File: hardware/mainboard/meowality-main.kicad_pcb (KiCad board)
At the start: 6 copper layers, 175 x 85 mm, 249 parts, among them J1 Micro_SD_Card_Det, J2 MINI_DP_SINK, J3 DEBUG, J4 USB_C_Receptacle, P1 M2_SOCKET_E, Q1 BSS138, Q10 BSS138, Q2 BSS138, Q3 BSS138, Q4 BSS138, Q5 BSS138, Q6 FDN340P, Q7 BSS138, SW1 SW_DIP_x04, SW2 SW_Push, SW3 SW_Push, SW4 SW_Push, SW5 SW_Push, SW6 SW_Push, U1 CP3225-100.000-3.3-25-X-T-TR, U10 MMC5983MA, U11 Si52112-B, U12 TPD4E02B04DQA, U13 TPD4E02B04DQA, U14 CBTL02043A, U15 FUSB302B11MPX, U16 USB3318, U19 ADP5070ACPZ, U2 AX3HAF1-135.0000T, U20 CAT4106HV4, U21 74LVC2T45DC, U3 AP6230xWU, U4 AP6230xWU, U5 SiC438, U6 AP6230xWU, U7 AP6230xWU, U8 TXS02612, U9 ICM-20789, X1 831056169, Y1 25MHz

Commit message: Initial 'floorplan' outline
Signed-off-by: gatecat <gatecat@ds0.me>
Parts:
- added C65: 10µ, Capacitor_SMD:C_1206_3216Metric, F.Cu at (327.7, 106.7)
- added C66: 100n, Capacitor_SMD:C_0402_1005Metric, F.Cu at (331.9, 107.1)
- added C77: 22µ, Capacitor_SMD:C_1206_3216Metric, F.Cu at (320.5, 110.7)
- added C78: 22µ, Capacitor_SMD:C_1206_3216Metric, F.Cu at (327.7, 103.3)
- added H1: MountingHole_Pad, MountingHole:MountingHole_2.7mm_M2.5_Pad_Via, F.Cu at (33.0, 117.0)
- added H10: MountingHole_Pad, MountingHole:MountingHole_2.7mm_M2.5_Pad_Via, F.Cu at (53.0, 63.0)
- added H2: MountingHole_Pad, MountingHole:MountingHole_2.7mm_M2.5_Pad_Via, F.Cu at (74.0, 132.0)
- added H3: MountingHole_Pad, MountingHole:MountingHole_2.7mm_M2.5_Pad_Via, F.Cu at (227.0, 132.0)
- added H4: MountingHole_Pad, MountingHole:MountingHole_2.7mm_M2.5_Pad_Via, F.Cu at (227.0, 63.0)
- added H5: MountingHole_Pad, MountingHole:MountingHole_2.7mm_M2.5_Pad_Via, F.Cu at (227.0, 97.5)
- added H6: MountingHole_Pad, MountingHole:MountingHole_2.7mm_M2.5_Pad_Via, F.Cu at (118.1, 132.1)
- added H7: MountingHole_Pad, MountingHole:MountingHole_2.7mm_M2.5_Pad_Via, F.Cu at (190.0, 63.0)
- added H8: MountingHole_Pad, MountingHole:MountingHole_2.7mm_M2.5_Pad_Via, F.Cu at (67.0, 105.5)
- added H9: MountingHole_Pad, MountingHole:MountingHole_2.7mm_M2.5_Pad_Via, F.Cu at (140.0, 63.0)
- added L9: 3.3µ, meowality:BWVS00606045, F.Cu at (321.3, 105.4)
- added R28: 31.6k, Resistor_SMD:R_0402_1005Metric, F.Cu at (327.7, 109.3)
- added R97: 10k, Resistor_SMD:R_0402_1005Metric, F.Cu at (324.8, 110.0)
- added U17: AP6230xWU, Package_TO_SOT_SMD:TSOT-23-6, F.Cu at (333.1, 103.9)
- LCD1, LCD2: moved to B.Cu
- moved SW6 354.4 mm to (56.0, 100.0)
- moved SW3 348.2 mm to (56.0, 76.0)
- moved SW4 342.2 mm to (56.0, 84.0)
- moved SW5 342.2 mm to (56.0, 92.0)
- moved LCD1 283.3 mm to (100.0, 87.0), turned to -90 degrees
- moved U14 276.8 mm to (55.0, 114.0)
- moved U9 275.3 mm to (121.0, 105.0)
- moved LCD2 240.1 mm to (160.0, 87.0), turned to -90 degrees
- moved C9 202.3 mm to (67.0, 96.0), turned to 90 degrees
- moved U4 125.7 mm to (166.0, 125.0)
- moved L2 114.8 mm to (159.0, 127.0)
- moved C21 114.2 mm to (166.0, 129.0)
- moved SOM1 66.0 mm to (221.3, 64.2), turned to 180 degrees
- moved SW1 48.5 mm to (216.0, 129.0)
- moved CAM2 29.5 mm to (110.0, 71.0)
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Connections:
- CAM1 pad 22: +3V3PS -> +3V3PL
- CAM2 pad 22: +3V3PS -> +3V3PL
- R63 pad 1: +3V3PS -> +3V3PL
- R64 pad 1: +3V3PS -> +3V3PL
- R65 pad 1: +3V3PS -> +3V3PL
- R66 pad 1: +3V3PS -> +3V3PL
- SOM1 pad 2D59: +3V3PS -> +3V3PL
- SOM1 pad 2D60: +3V3PS -> +3V3PL
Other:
- board size 175 x 85 mm -> 200 x 75 mm

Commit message: Placement snapshot
Signed-off-by: gatecat <gatecat@ds0.me>
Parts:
- moved U8 347.1 mm to (70.6, 78.5)
- moved U15 264.0 mm to (78.1, 122.6)
- moved U16 250.2 mm to (92.4, 122.0)
- moved C10 229.7 mm to (73.5, 89.2), turned to -90 degrees
- moved C13 221.0 mm to (71.0, 89.2), turned to -90 degrees
- moved C15 211.5 mm to (75.8, 89.3), turned to -90 degrees
- moved U5 197.1 mm to (78.1, 87.0)
- moved L3 191.9 mm to (79.2, 97.2)
- moved C18 150.9 mm to (152.0, 123.2), turned to 180 degrees
- moved C12 145.8 mm to (147.0, 124.8), turned to 180 degrees
- moved R9 143.7 mm to (155.8, 128.0), turned to 90 degrees
- moved U2 136.4 mm to (139.5, 95.5)
- moved R10 135.8 mm to (155.8, 125.8), turned to 90 degrees
- moved C17 132.7 mm to (167.0, 123.2), turned to 180 degrees
- moved C30 126.1 mm to (182.0, 123.2), turned to 180 degrees
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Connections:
- U5 pad 12: /Power/SiC_V_{DD} -> Net-(C16-Pad2)
- U5 pad 15: (no net) -> /Power/SiC_V_{DD}

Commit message: Placement snapshot 2
Signed-off-by: gatecat <gatecat@ds0.me>
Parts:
- moved R80 333.3 mm to (86.2, 72.2)
- moved R79 325.3 mm to (86.2, 75.8)
- moved R76 318.9 mm to (101.2, 81.5), turned to 90 degrees
- moved R77 317.3 mm to (100.0, 81.5), turned to 90 degrees
- moved R78 315.1 mm to (86.2, 73.5)
- moved R87 314.8 mm to (99.0, 81.5), turned to -90 degrees
- moved L6 313.8 mm to (97.2, 70.0), turned to 90 degrees
- moved R75 313.5 mm to (95.8, 88.8)
- moved R88 311.0 mm to (103.0, 77.5)
- moved C73 308.6 mm to (103.0, 76.0)
- moved C70 308.6 mm to (96.0, 84.8), turned to 90 degrees
- moved C75 308.2 mm to (109.0, 68.5), turned to 90 degrees
- moved R86 304.6 mm to (94.8, 82.2), turned to 90 degrees
- moved R82 304.1 mm to (103.5, 81.0), turned to 90 degrees
- moved C74 303.6 mm to (91.8, 82.2)
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
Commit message: Placement snapshot 3
Signed-off-by: gatecat <gatecat@ds0.me>
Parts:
- removed the C65 at (302.2, 142.7)
- removed the C66 at (290.2, 153.4)
- removed Q4: BSS138, Package_TO_SOT_SMD:SOT-23
- removed Q6: FDN340P, Package_TO_SOT_SMD:SOT-23
- removed the R28 at (289.4, 157.7)
- TP2, TP3: moved to B.Cu
- moved R32 359.0 mm to (79.5, 64.2), turned to -90 degrees
- moved D7 354.4 mm to (73.5, 61.0)
- moved C40 345.9 mm to (70.8, 73.5), turned to 180 degrees
- moved D10 343.1 mm to (64.5, 61.0)
- moved R33 331.1 mm to (78.0, 64.2), turned to -90 degrees
- moved D9 331.0 mm to (69.0, 61.0)
- moved R23 329.3 mm to (113.8, 95.5), turned to 90 degrees
- moved R36 328.5 mm to (101.0, 97.2), turned to 180 degrees
- moved C42 326.8 mm to (74.8, 78.2), turned to -90 degrees
- moved R25 325.1 mm to (110.5, 103.8), turned to 90 degrees
- moved D6 324.3 mm to (78.0, 61.0)
- moved R37 324.3 mm to (101.0, 95.8), turned to 180 degrees
- moved C37 323.2 mm to (118.0, 101.0)
- moved C44 317.0 mm to (104.3, 98.8)
- moved C36 315.4 mm to (118.5, 99.5)
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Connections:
- C46 pad 1: Net-(C46-Pad1) -> unconnected-(C46-Pad1)
- C46 pad 2: GND -> unconnected-(C46-Pad2)
- C47 pad 1: Net-(C46-Pad1) -> unconnected-(C47-Pad1)
- C47 pad 2: GND -> unconnected-(C47-Pad2)
- D10 pad 2: Net-(D10-Pad2) -> unconnected-(D10-Pad2)
- FB2 pad 2: Net-(C46-Pad1) -> Net-(FB2-Pad2)
- R70 pad 1: Net-(D10-Pad2) -> unconnected-(R70-Pad1)
- R70 pad 2: PL_LED3B -> unconnected-(R70-Pad2)
- U11 pad 1: Net-(C46-Pad1) -> Net-(FB2-Pad2)
- U11 pad 10: Net-(C46-Pad1) -> Net-(FB2-Pad2)

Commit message: All parts placed
Signed-off-by: gatecat <gatecat@ds0.me>
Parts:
- R52, R53: value 5.1k -> DNP
- TP1: moved to B.Cu
- moved R42 374.5 mm to (62.0, 73.2), turned to -90 degrees
- moved R39 373.3 mm to (65.8, 83.2)
- moved R96 373.2 mm to (58.5, 64.2), turned to -90 degrees
- moved R71 369.1 mm to (64.5, 64.2), turned to -90 degrees
- moved R70 363.9 mm to (65.8, 64.2), turned to -90 degrees
- moved C35 359.3 mm to (66.0, 77.2), turned to 90 degrees
- moved R41 357.9 mm to (84.2, 130.8)
- moved R95 355.5 mm to (59.8, 64.2), turned to -90 degrees
- moved R69 350.7 mm to (67.8, 64.2), turned to -90 degrees
- moved R40 348.8 mm to (74.5, 64.2), turned to -90 degrees
- moved R73 348.6 mm to (61.0, 64.2), turned to -90 degrees
- moved R49 346.5 mm to (72.0, 64.2), turned to -90 degrees
- moved R72 342.8 mm to (63.2, 64.2), turned to -90 degrees
- moved R67 342.3 mm to (70.2, 64.2), turned to -90 degrees
- moved R48 341.6 mm to (73.2, 64.2), turned to -90 degrees
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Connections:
- C46 pad 1: unconnected-(C46-Pad1) -> Net-(FB2-Pad2)
- C46 pad 2: unconnected-(C46-Pad2) -> GND
- C47 pad 1: unconnected-(C47-Pad1) -> Net-(FB2-Pad2)
- C47 pad 2: unconnected-(C47-Pad2) -> GND
- C54 pad 1: /IO/SSTXC1+ -> /IO/SSTX1+
- C55 pad 1: /IO/SSTXC1- -> /IO/SSTX1-
- C56 pad 1: /IO/SSTXC2+ -> /IO/SSTX2+
- C57 pad 1: /IO/SSTXC2- -> /IO/SSTX2-
- D10 pad 2: unconnected-(D10-Pad2) -> Net-(D10-Pad2)
- R70 pad 1: unconnected-(R70-Pad1) -> Net-(D10-Pad2)
- R70 pad 2: unconnected-(R70-Pad2) -> PL_LED3B
- U5 pad 12: Net-(C16-Pad2) -> /Power/SiC_V_{DD}
- U5 pad 15: /Power/SiC_V_{DD} -> (no net)

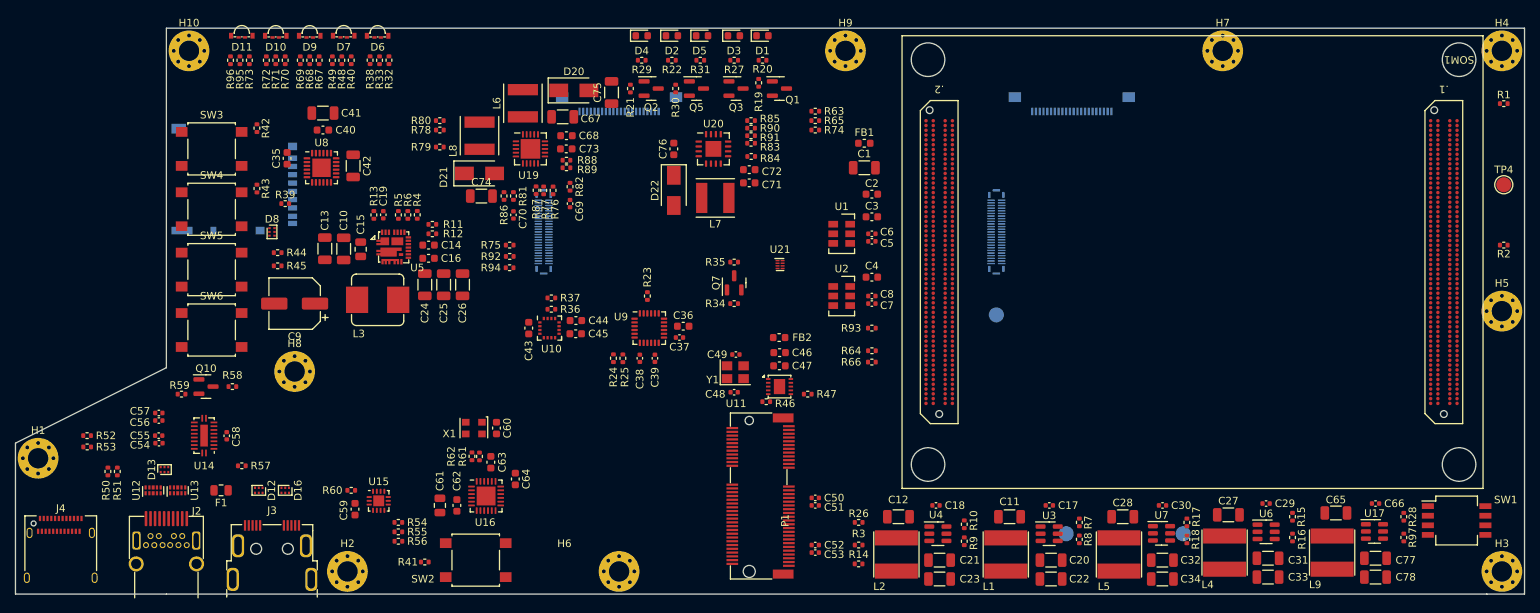
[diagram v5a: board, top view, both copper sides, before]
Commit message: Tidy up silk
Signed-off-by: gatecat <gatecat@ds0.me>
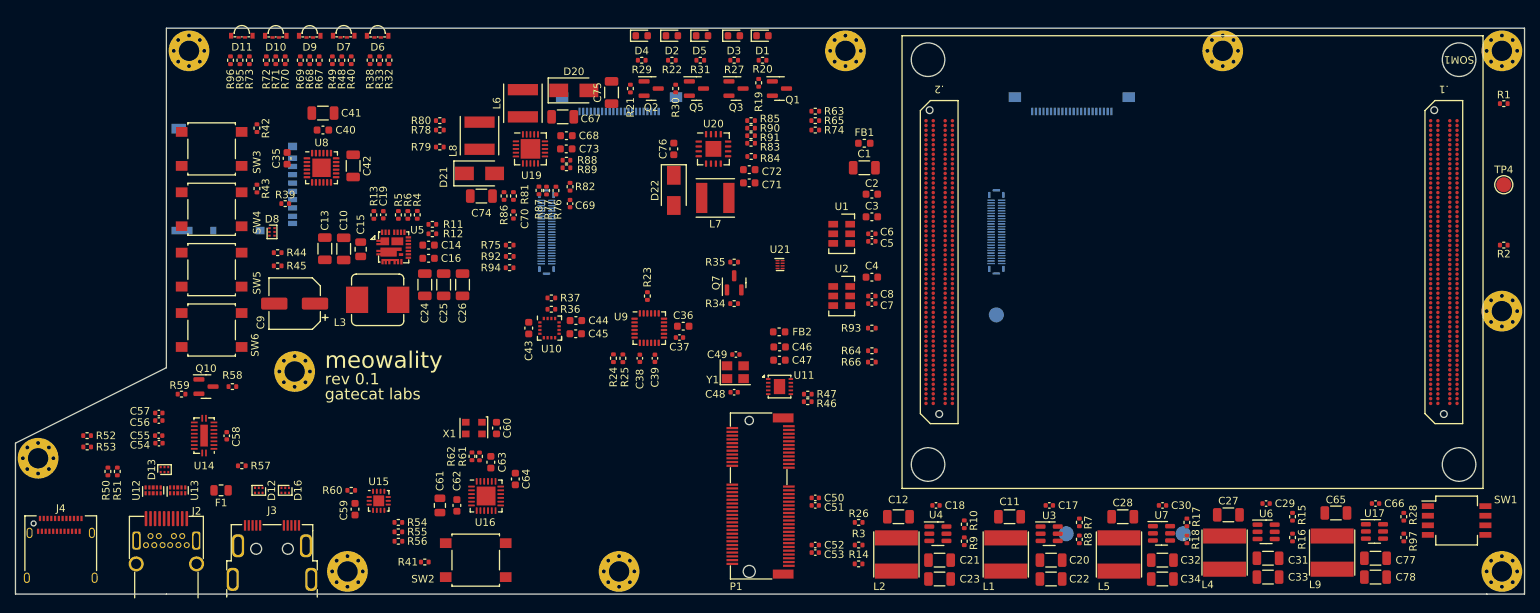
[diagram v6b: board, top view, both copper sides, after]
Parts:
- moved R46 5.50 mm to (135.0, 109.5)
- moved C46 0.75 mm to (131.3, 102.2)
- moved C47 0.75 mm to (131.2, 104.0)
- moved FB2 0.75 mm to (131.2, 100.2)
- moved LCD1 0.38 mm to (100.4, 87.0)
- moved R76 0.38 mm to (101.6, 81.5)
- moved R77 0.38 mm to (100.4, 81.5)
- moved R87 0.38 mm to (99.4, 81.5)
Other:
- board text added: "gatecat labs"
- board text added: "meowality"
- board text added: "rev 0.1"

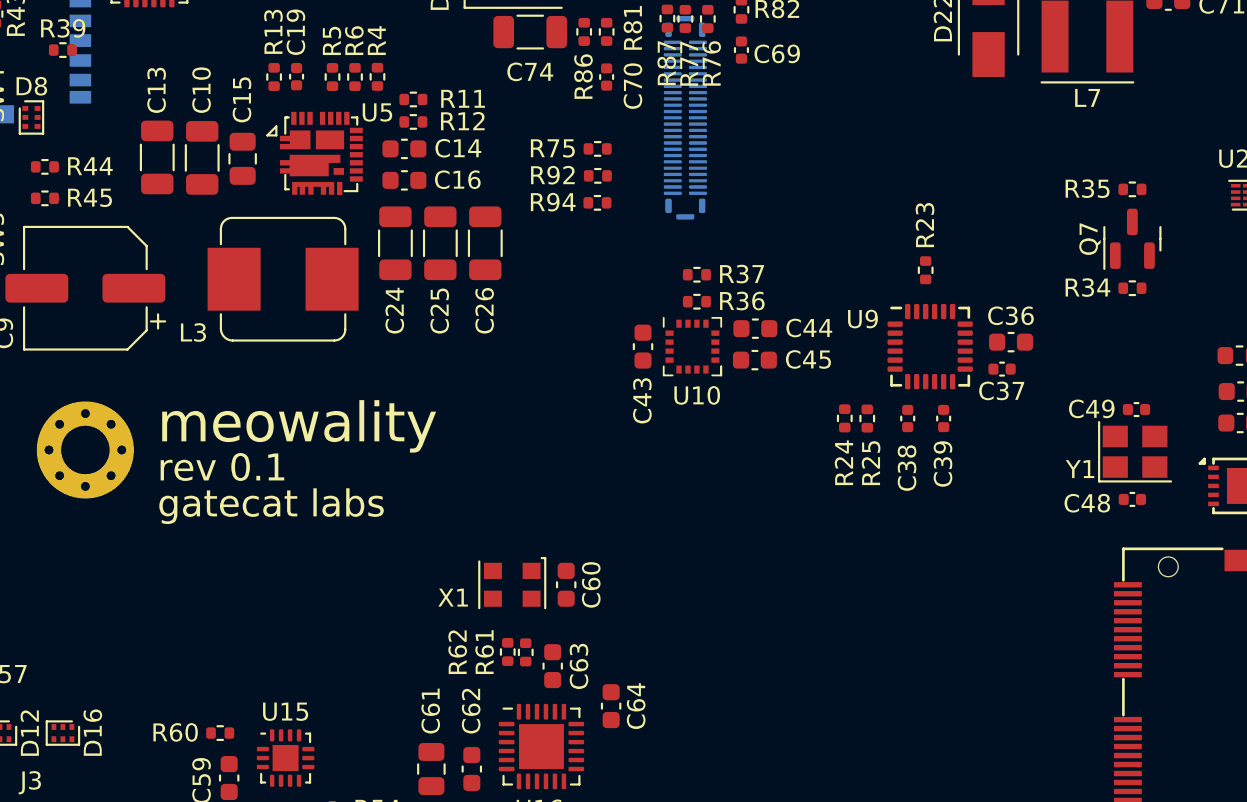
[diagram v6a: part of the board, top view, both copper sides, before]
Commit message: Add TVS on 5V and Vbus
Signed-off-by: gatecat <gatecat@ds0.me>
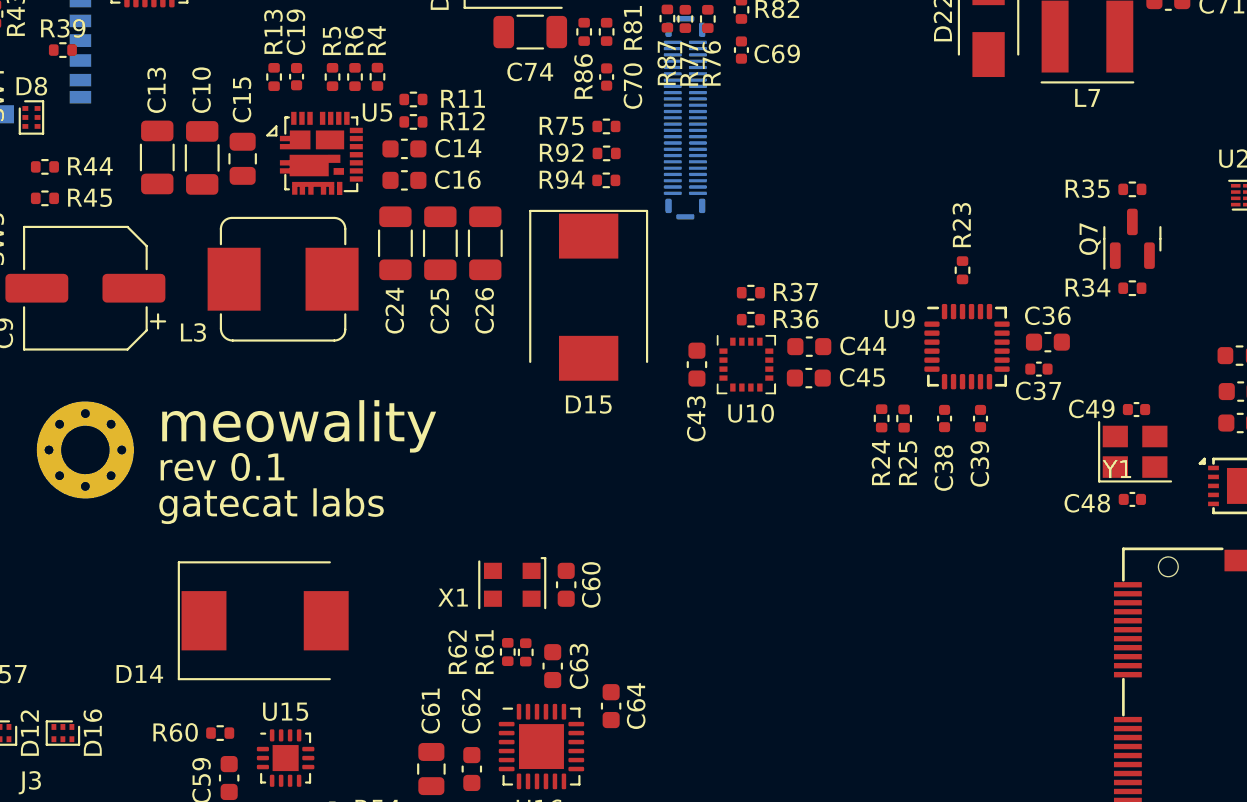
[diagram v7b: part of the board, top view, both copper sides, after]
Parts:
- added D14: SMDJ22CA, Diode_SMD:D_SMC, F.Cu at (77.0, 115.0)
- added D15: 1.5SMC6.8A, Diode_SMD:D_SMC, F.Cu at (95.0, 97.0)
- moved C43 3.16 mm to (101.0, 100.8)
- moved C44 3.16 mm to (107.3, 99.8)
- moved C45 3.16 mm to (107.2, 101.5)
- moved R36 3.16 mm to (104.0, 98.2)
- moved R37 3.16 mm to (104.0, 96.8)
- moved U10 3.16 mm to (103.8, 100.8)
- moved C36 2.05 mm to (120.5, 99.5)
- moved C37 2.05 mm to (120.0, 101.0)
- moved C38 2.05 mm to (114.8, 103.8)
- moved C39 2.05 mm to (116.8, 103.8)
- moved R23 2.05 mm to (115.8, 95.5)
- moved R24 2.05 mm to (111.3, 103.7)
- moved R25 2.05 mm to (112.5, 103.8)
- moved U9 2.05 mm to (116.0, 99.8)
- moved R94 1.34 mm to (96.0, 90.5)
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
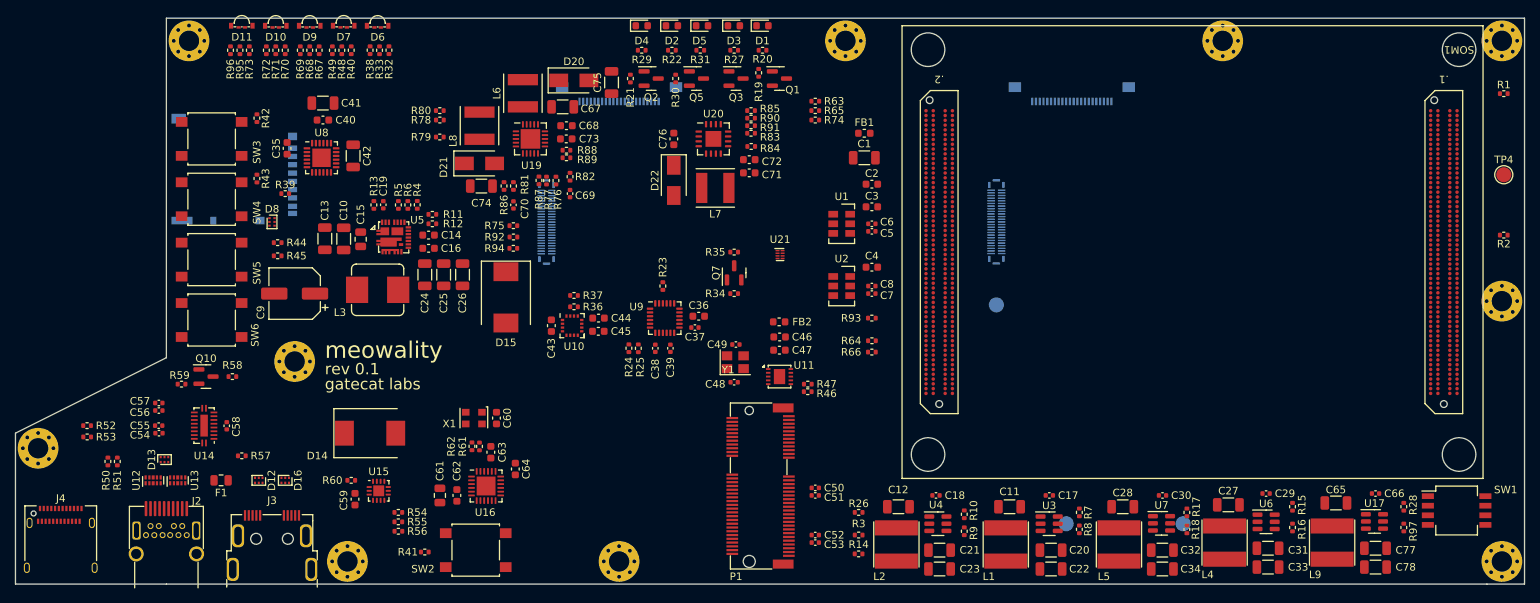
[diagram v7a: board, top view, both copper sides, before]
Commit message: Mechanical updates; add cam clk connectors
Signed-off-by: gatecat <gatecat@ds0.me>
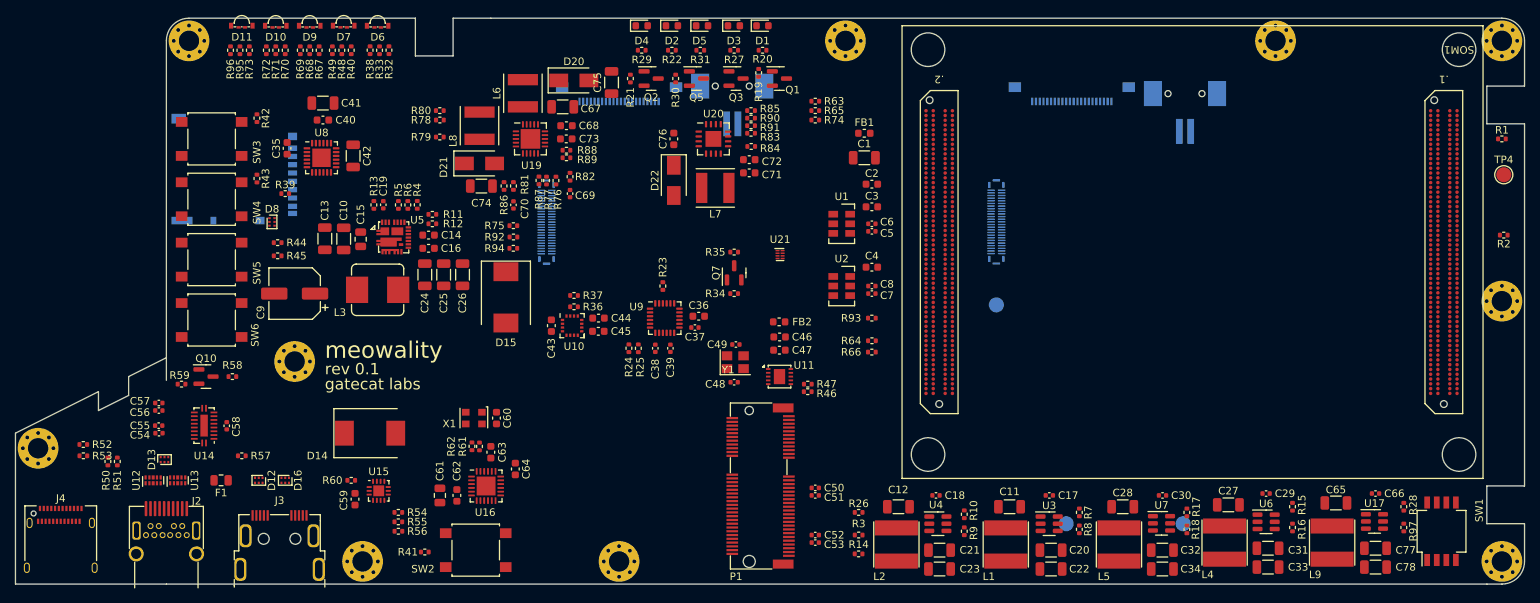
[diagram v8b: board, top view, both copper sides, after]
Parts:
- added J5: Conn_01x02, meowality:TE-292227-2, B.Cu at (125.0, 69.0)
- added J6: Conn_01x02, meowality:TE-292227-2, B.Cu at (185.0, 70.0)
- moved H7 7.00 mm to (197.0, 63.0)
- moved R1 6.01 mm to (227.0, 76.0)
- moved SW1 3.40 mm to (219.0, 128.0), turned to 90 degrees
- moved R52 2.55 mm to (39.0, 116.5)
- moved R53 2.55 mm to (39.0, 118.0)
- moved H2 2.00 mm to (76.0, 132.0)
- moved J3 1.00 mm to (65.0, 129.0)
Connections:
- SOM1 pad 2C50: unconnected-(SOM1-Pad2C50) -> CAM_CLK_L
- SOM1 pad 2C51: unconnected-(SOM1-Pad2C51) -> CAM_CLK_R
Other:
- outline, holes or cut-outs redrawn
